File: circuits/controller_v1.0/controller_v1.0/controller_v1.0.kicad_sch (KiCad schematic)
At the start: 11 parts

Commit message: Some fixes to the bioreactor frontend
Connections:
- net Earth: now also U?.1 (ADDR)
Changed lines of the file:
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@@
+    (stroke (width 0) (type default) (color 0 0 0 0))
+  )
+  (wire (pts (xy 106.68 115.57) (xy 116.84 115.57))
     (stroke (width 0) (type default) (color 0 0 0 0))
   )
@@
     (stroke (width 0) (type default) (color 0 0 0 0))
   )
+  (wire (pts (xy 106.68 110.49) (xy 106.68 115.57))
+    (stroke (width 0) (type default) (color 0 0 0 0))
+  )

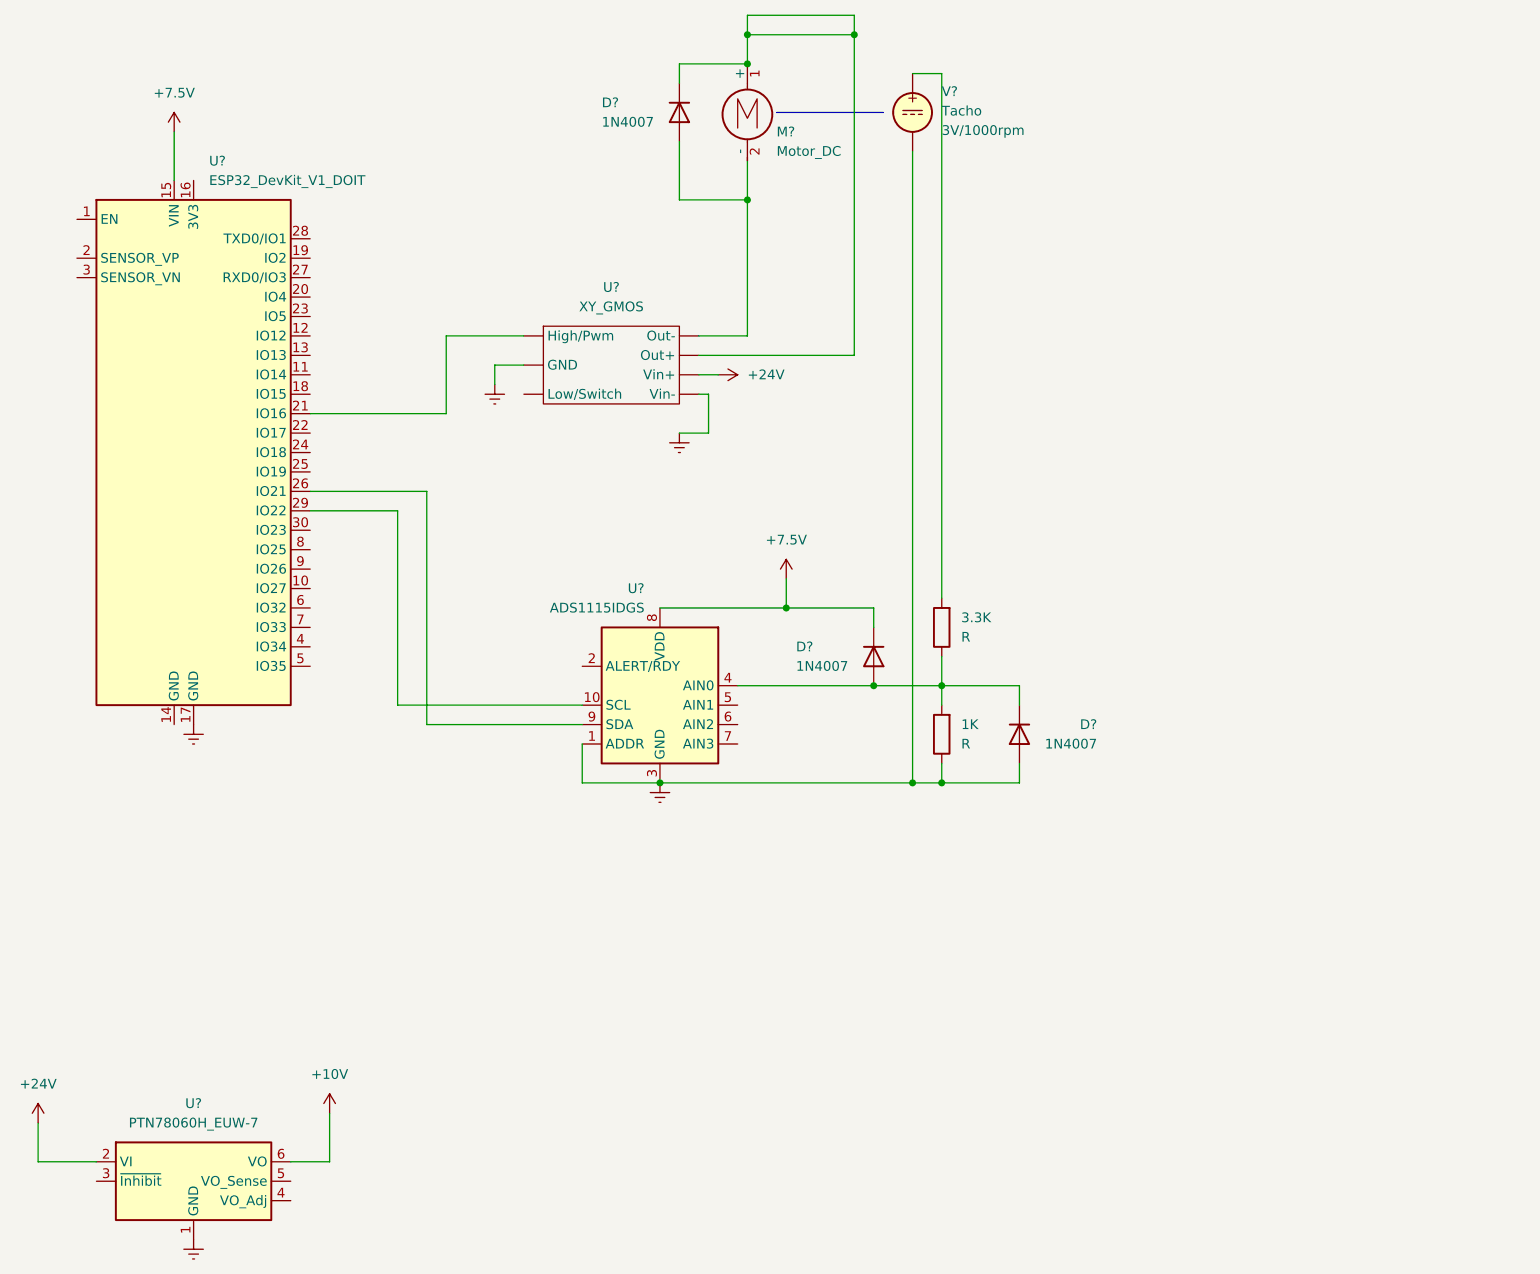
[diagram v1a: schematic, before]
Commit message: Updated the Controller sketch and added MAX31865 KiCad symbol
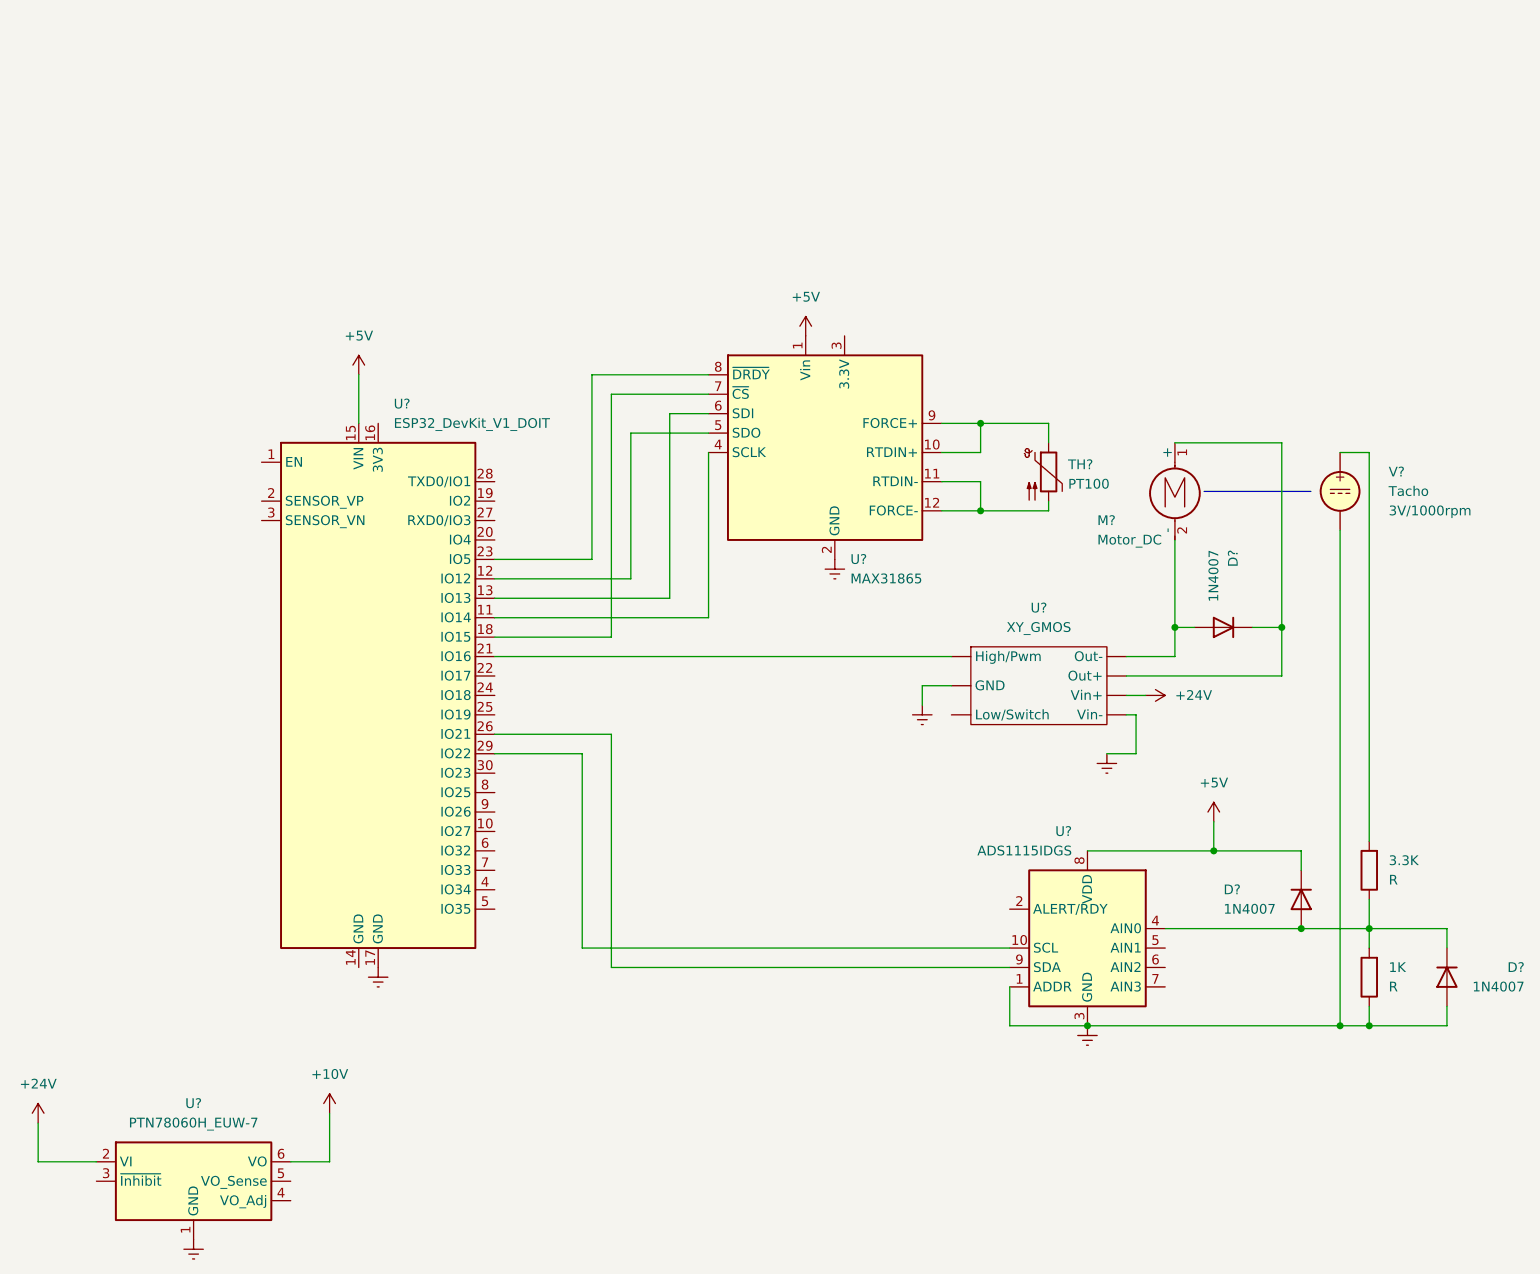
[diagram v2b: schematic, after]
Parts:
- added TH?: PT100, symbol Sensor_Temperature:PT100
- added U?: MAX31865, symbol SysMo:MAX31865
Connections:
- net Earth: now also U?.2 (GND)
- net at U?.11 (IO14): now also U?.4 (SCLK)
- net at U?.12 (IO12): now also U?.5 (SDO)
- net at U?.13 (IO13): now also U?.6 (SDI)
- net at U?.18 (IO15): now also U?.7 (~{CS})
- net at U?.23 (IO5): now also U?.8 (~{DRDY})
- net +7.5V renamed +5V
- net +5V: now also U?.1 (Vin)
- new net: TH?.1, U?.10 (RTDIN+), U?.9 (FORCE+)
- new net: TH?.2, U?.11 (RTDIN-), U?.12 (FORCE-)
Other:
- moved on the sheet: 1K, 3.3K, D?, M?, U?, V?
